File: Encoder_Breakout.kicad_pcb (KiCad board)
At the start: 2 copper layers, 57 x 33.5 mm, 8 parts, among them J1 5-104363-1, J2 Conn_02x07_Odd_Even, J5 5-104935-3, J6 5-104363-1

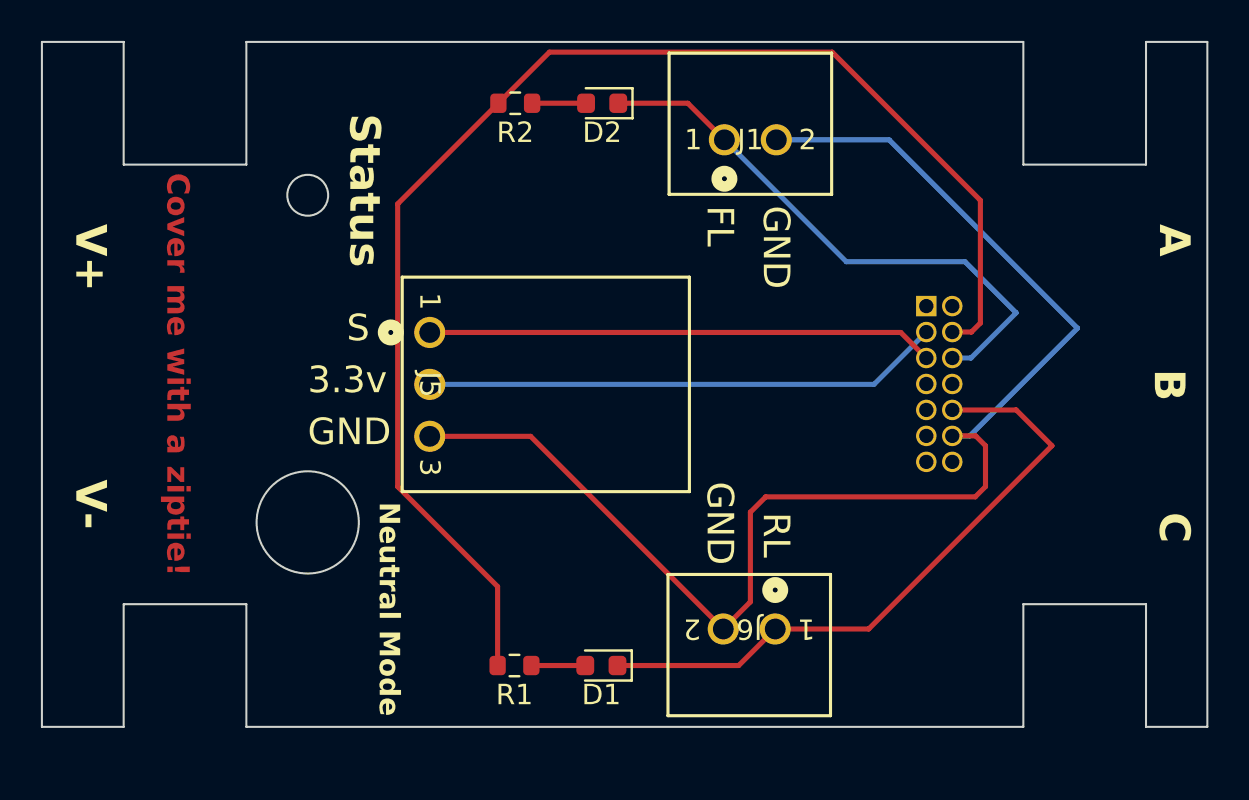
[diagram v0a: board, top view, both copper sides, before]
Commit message: Remove limit switches
Signed-off-by: Colin <cfinn68916@gmail.com>
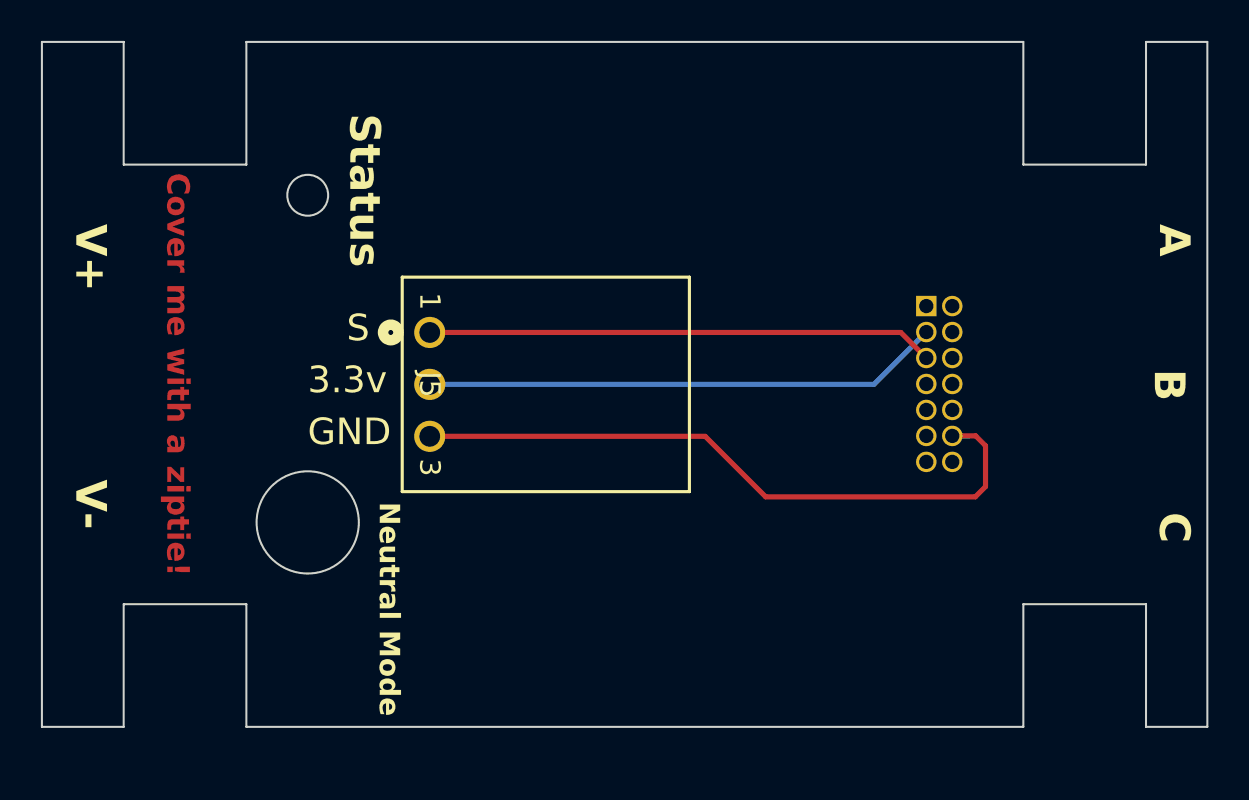
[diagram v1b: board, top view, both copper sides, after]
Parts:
- removed D1, D2: LED, LED_SMD:LED_0603_1608Metric
- removed J1, J6: 5-104363-1, footprints:CONN_5-104363-1_TYCO
- removed R1, R2: 270Ω, Resistor_SMD:R_0603_1608Metric
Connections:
- J2 pad 10: Net-(D1-K) -> unconnected-(J2-Pin_10-Pad10)
- J2 pad 4: +5V -> unconnected-(J2-Pin_4-Pad4)
- J2 pad 6: Net-(D2-K) -> unconnected-(J2-Pin_6-Pad6)
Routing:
- net +5V: track 66.7 -> 0.00 mm
- net GND: track 67.2 -> 33.3 mm
- net Net-(D1-K): track 31.3 -> 0.00 mm
- net Net-(D2-K): track 27.7 -> 0.00 mm
- net Net-(D2-A): track 2.64 -> 0.00 mm
- net Net-(D1-A): track 2.64 -> 0.00 mm
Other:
- board text removed: "FL"
- board text removed: "RL"
